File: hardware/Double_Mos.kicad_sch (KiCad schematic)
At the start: 12 parts, among them U4 AOZ5276QI, U5 AOZ5276QI

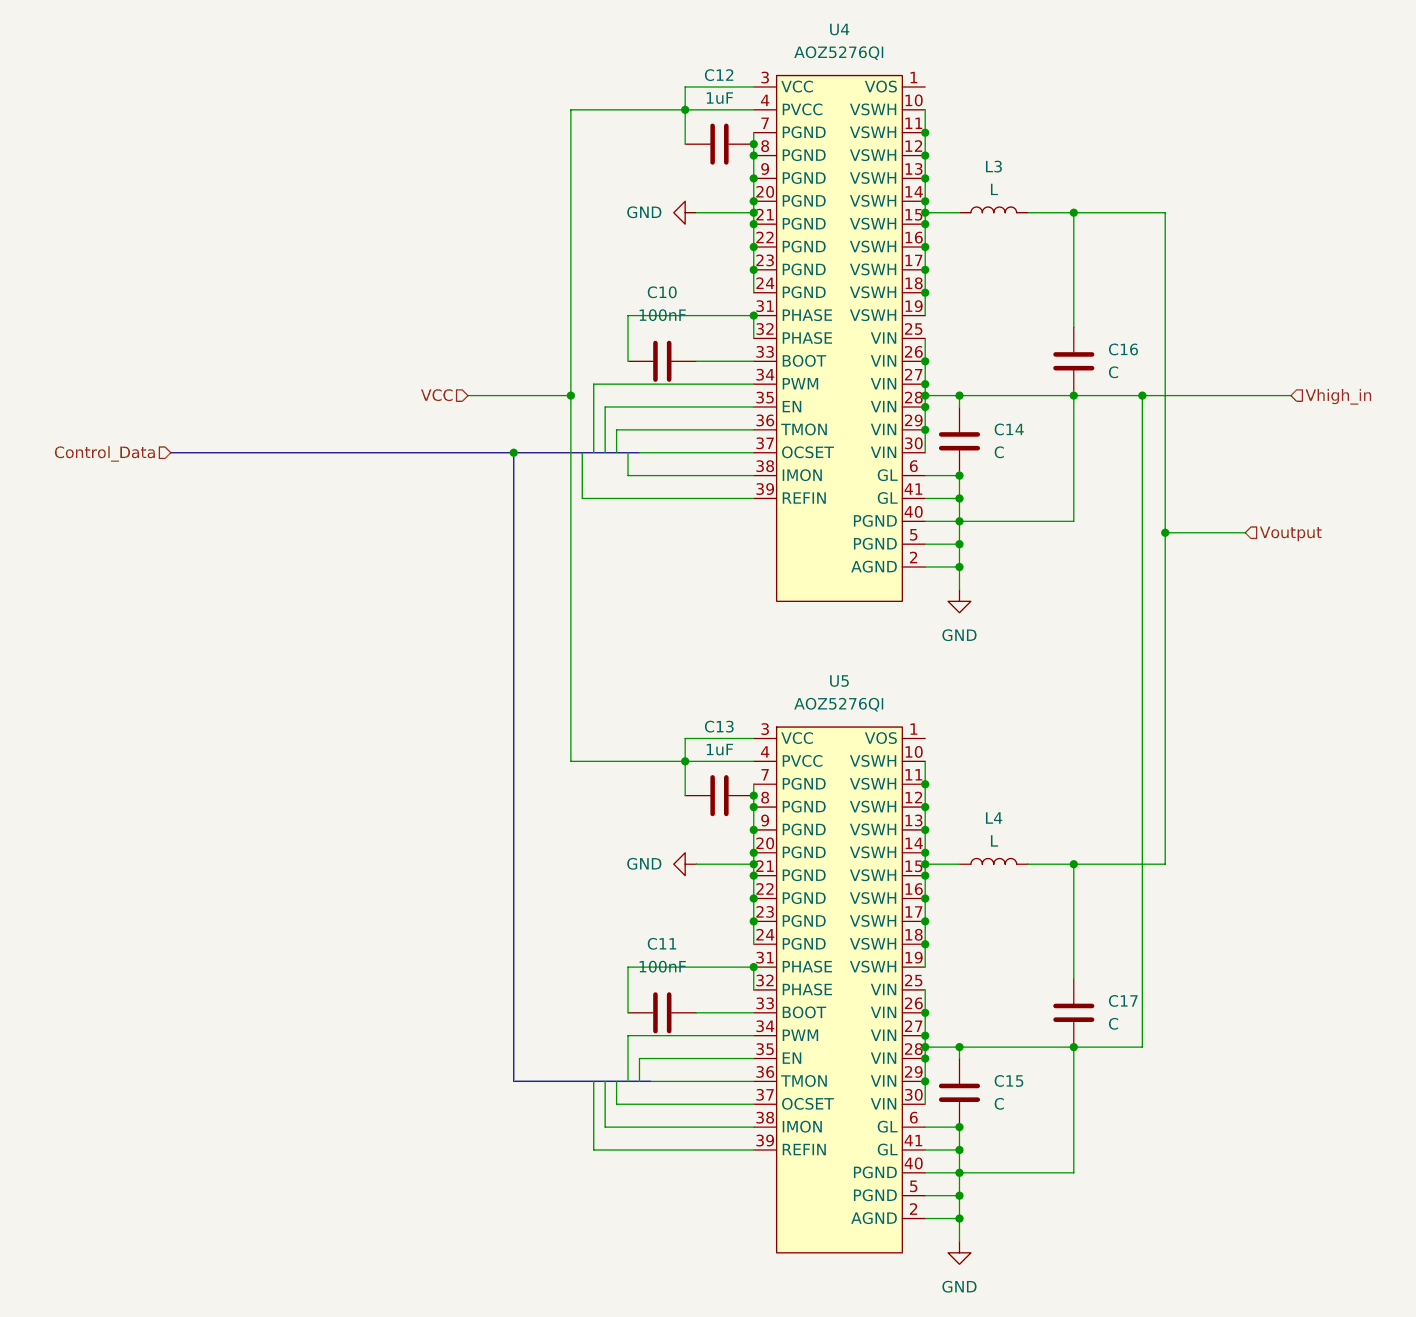
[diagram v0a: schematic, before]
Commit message: chore: redirect sub-schematic from untitled to Double_Mos
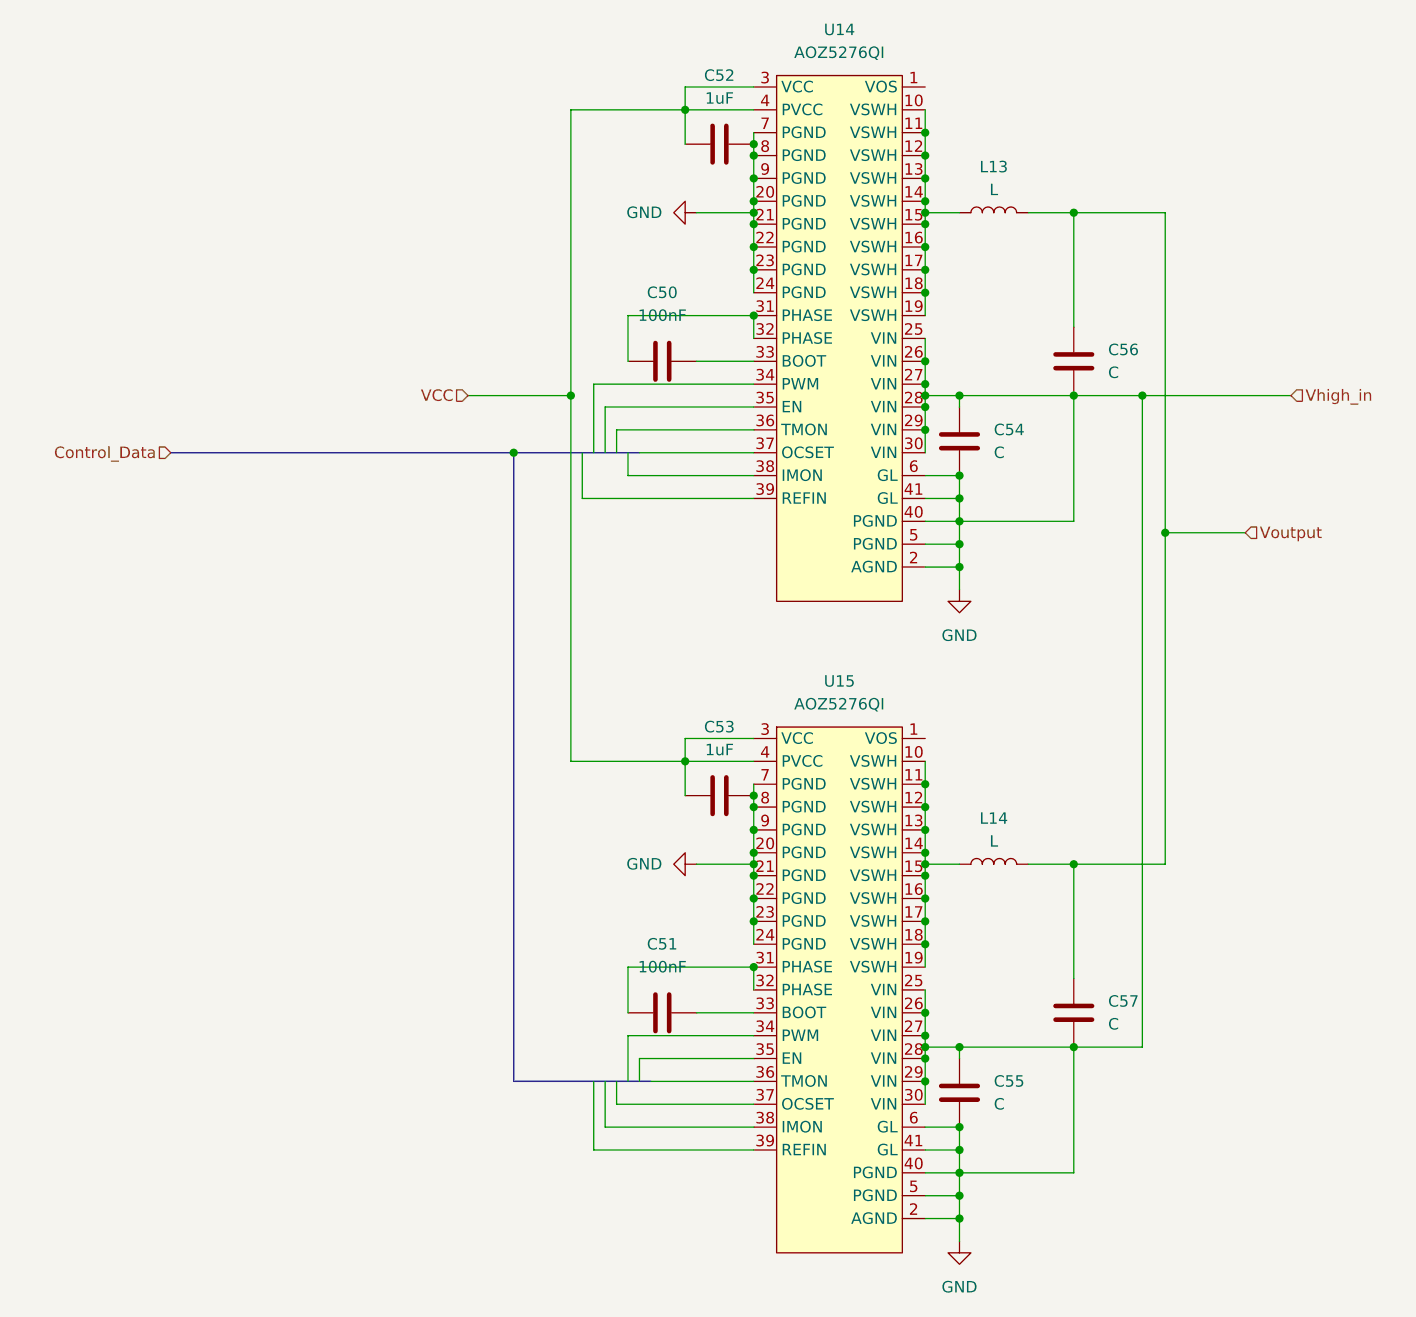
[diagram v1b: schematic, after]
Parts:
- renumbered C10 to C50, C11 to C51, C12 to C52, C13 to C53, C14 to C54, C15 to C55, C16 to C56, C17 to C57, L3 to L13, L4 to L14, U4 to U14, U5 to U15
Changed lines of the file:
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@@
 		(dnp no)
 		(fields_autoplaced yes)
-		(property "Reference" "U4"
+		(property "Reference" "U14"
 			(at 127.635 31.75 0)
 			(effects
@@
 		(dnp no)
 		(fields_autoplaced yes)
-		(property "Reference" "#PWR09"
+		(property "Reference" "#PWR029"
 			(at 140.97 172.72 0)
 			(effects
@@
 		(dnp no)
 		(fields_autoplaced yes)
-		(property "Reference" "C11"
+		(property "Reference" "C51"
 			(at 107.95 133.35 90)
 			(effects
@@
 		(dnp no)
 		(fields_autoplaced yes)
-		(property "Reference" "#PWR06"
+		(property "Reference" "#PWR026"
 			(at 105.41 52.07 0)
 			(effects
@@
 		(dnp no)
 		(fields_autoplaced yes)
-		(property "Reference" "C13"
+		(property "Reference" "C53"
 			(at 114.3 109.22 90)
 			(effects
@@
 		(dnp no)
 		(fields_autoplaced yes)
-		(property "Reference" "U5"
+		(property "Reference" "U15"
 			(at 127.635 104.14 0)
 			(effects
@@
 		(dnp no)
 		(fields_autoplaced yes)
-		(property "Reference" "#PWR08"
+		(property "Reference" "#PWR028"
 			(at 140.97 100.33 0)
 			(effects
@@
 		(dnp no)
 		(fields_autoplaced yes)
-		(property "Reference" "#PWR07"
+		(property "Reference" "#PWR027"
 			(at 105.41 124.46 0)
 			(effects
@@
 		(dnp no)
 		(fields_autoplaced yes)
-		(property "Reference" "C15"
+		(property "Reference" "C55"
 			(at 144.78 148.5899 0)
 			(effects
@@
 		(dnp no)
 		(fields_autoplaced yes)
-		(property "Reference" "C17"
+		(property "Reference" "C57"
 			(at 157.48 139.6999 0)
 			(effects
@@
 		(dnp no)
 		(fields_autoplaced yes)
-		(property "Reference" "L4"
+		(property "Reference" "L14"
 			(at 144.78 119.38 90)
 			(effects
@@
 		(dnp no)
 		(fields_autoplaced yes)
-		(property "Reference" "C10"
+		(property "Reference" "C50"
 			(at 107.95 60.96 90)
 			(effects
@@
 		(dnp no)
 		(fields_autoplaced yes)
-		(property "Reference" "C12"
+		(property "Reference" "C52"
 			(at 114.3 36.83 90)
 			(effects
@@
 		(dnp no)
 		(fields_autoplaced yes)
-		(property "Reference" "C16"
+		(property "Reference" "C56"
 			(at 157.48 67.3099 0)
 			(effects
@@
 		(dnp no)
 		(fields_autoplaced yes)
-		(property "Reference" "L3"
+		(property "Reference" "L13"
 			(at 144.78 46.99 90)
 			(effects
@@
 		(dnp no)
 		(fields_autoplaced yes)
-		(property "Reference" "C14"
+		(property "Reference" "C54"
 			(at 144.78 76.1999 0)
 			(effects

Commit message: chore: update project references
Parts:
- renumbered C50 to C14001, C51 to C14002, C52 to C14003, C53 to C14004, C54 to C14005, C55 to C14006, C56 to C14007, C57 to C14008, L13 to L14001, L14 to L14002, U14 to U14001, U15 to U14002
